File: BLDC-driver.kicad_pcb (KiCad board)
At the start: 2 copper layers, 52.2 x 52.2 mm, 107 parts, among them J1 Conn_01x06, J2 Conn_01x06, J3 Conn_01x02, J4 Encoder, Q1 FDMS8018, Q2 FDMS8018, Q3 FDMS8018, Q4 FDMS8018, Q5 FDMS8018, Q6 FDMS8018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

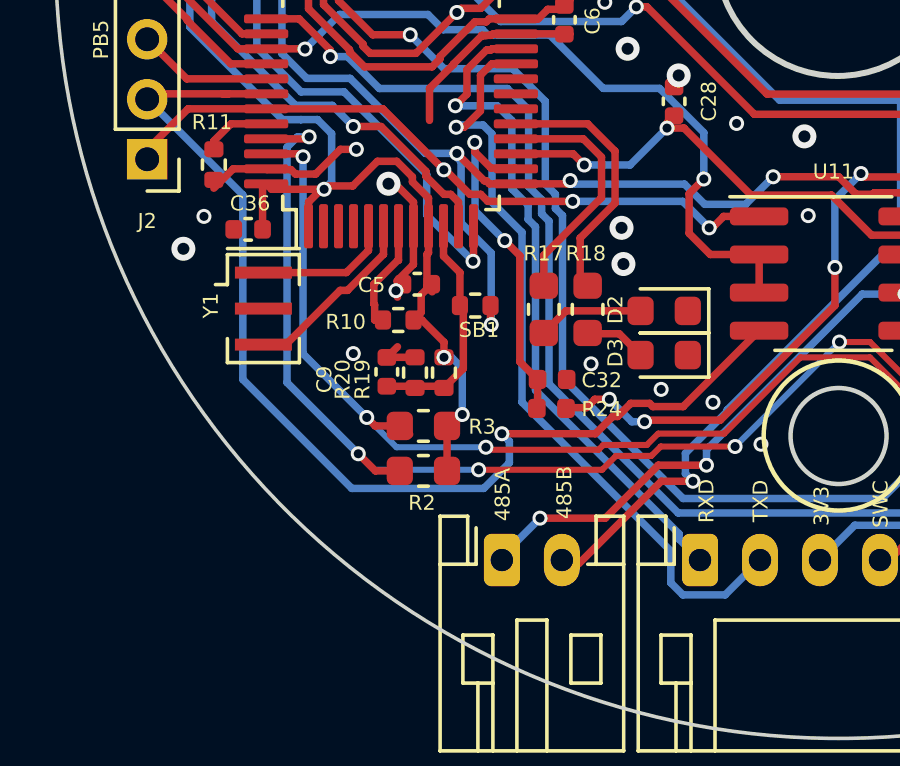
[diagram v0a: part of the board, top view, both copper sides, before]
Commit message: Update BOM, change crystal to 16Mhz
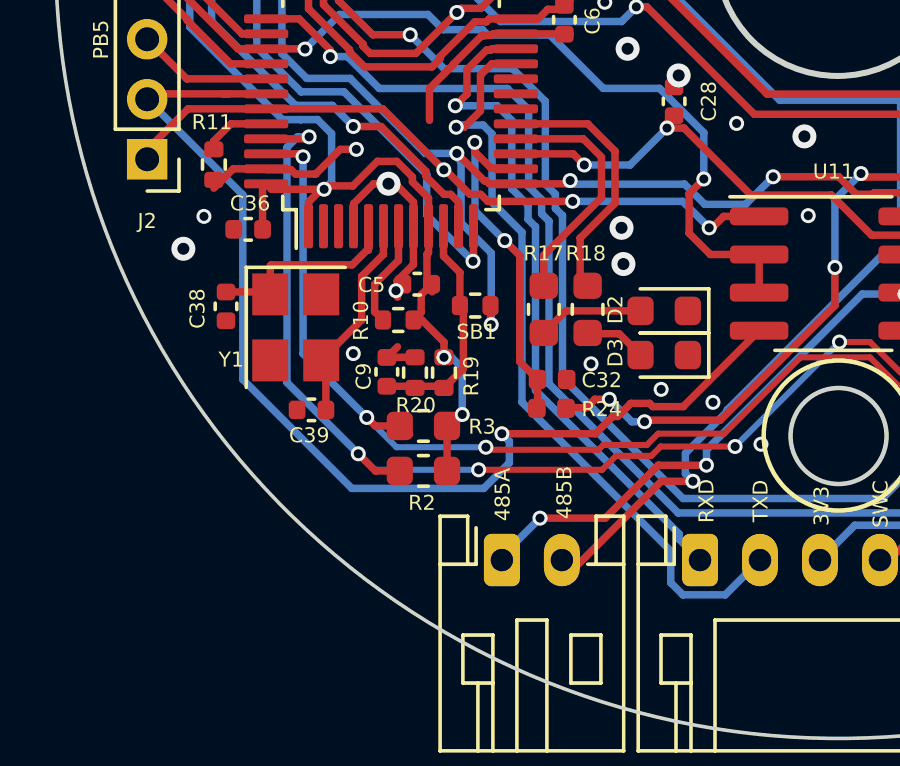
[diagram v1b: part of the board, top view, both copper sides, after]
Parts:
- added C38: 22p, Capacitor_SMD:C_0402_1005Metric, F.Cu at (176.3, 134.8)
- added C39: 22p, Capacitor_SMD:C_0402_1005Metric, F.Cu at (179.2, 138.3)
- Y1: value 8MHz -> 16MHz; footprint Crystal:Resonator_SMD_muRata_CSTxExxV-3Pin_3.0x1.1mm -> Crystal:Crystal_SMD_3225-4Pin_3.2x2.5mm
- moved Y1 1.25 mm to (178.6, 135.5)
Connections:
- U2 pad 18: Net-(U2-Pad18) -> (no net)
- U2 pad 19: Net-(U2-Pad19) -> (no net)
- U2 pad 2: Net-(U2-Pad2) -> (no net)
- U2 pad 20: Net-(U2-Pad20) -> (no net)
- U2 pad 25: Net-(U2-Pad25) -> (no net)
- U2 pad 26: Net-(U2-Pad26) -> (no net)
- U2 pad 3: Net-(U2-Pad3) -> (no net)
- U2 pad 32: /CANRX -> (no net)
- U2 pad 33: /CANTX -> (no net)
- U2 pad 4: Net-(U2-Pad4) -> GND
- U7 pad 4: Net-(U7-Pad4) -> (no net)
- Y1 pad 2: GND -> (no net)
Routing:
- net Net-(C38-Pad2): track 4.62 -> 7.52 mm
- net GND: track 54.5 -> 56.7 mm
- net Net-(C39-Pad2): track 6.19 -> 7.05 mm

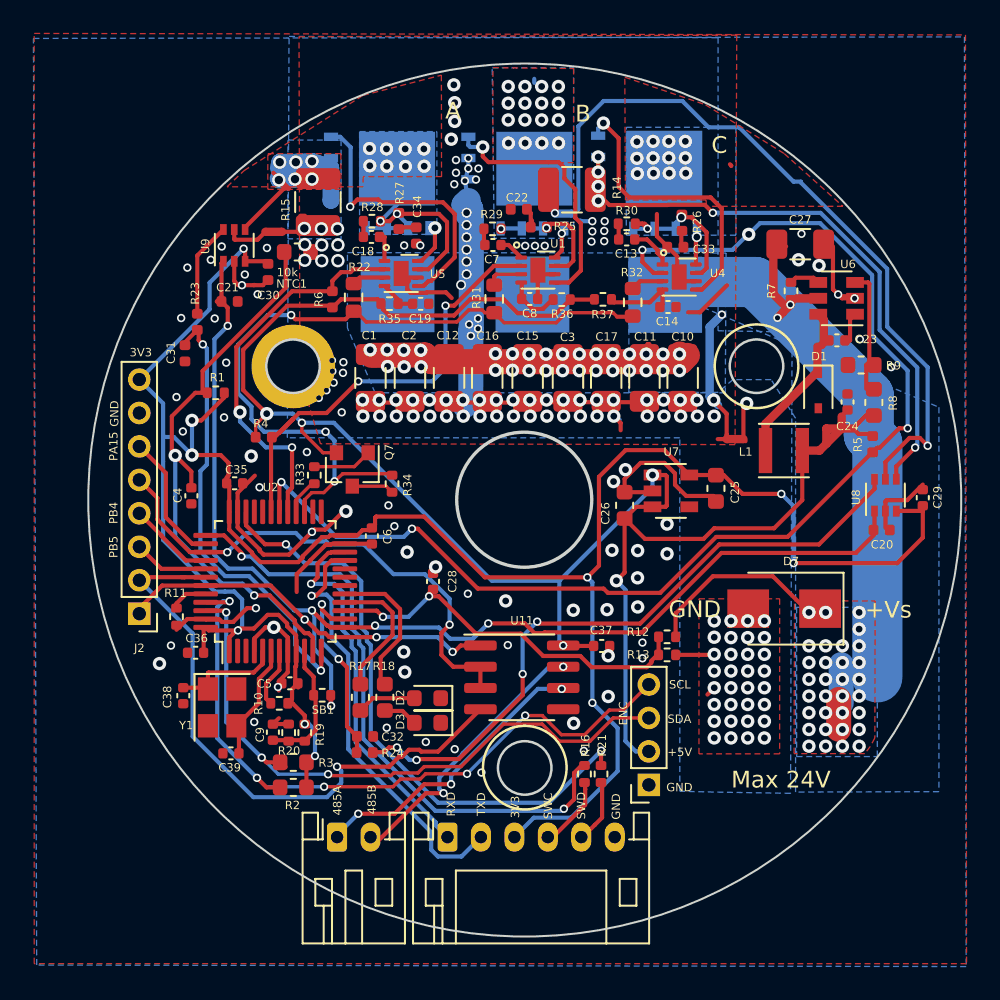
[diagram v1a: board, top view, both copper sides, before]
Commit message: Add encoder FFC connector, change NCP drivers to JLC sourceable
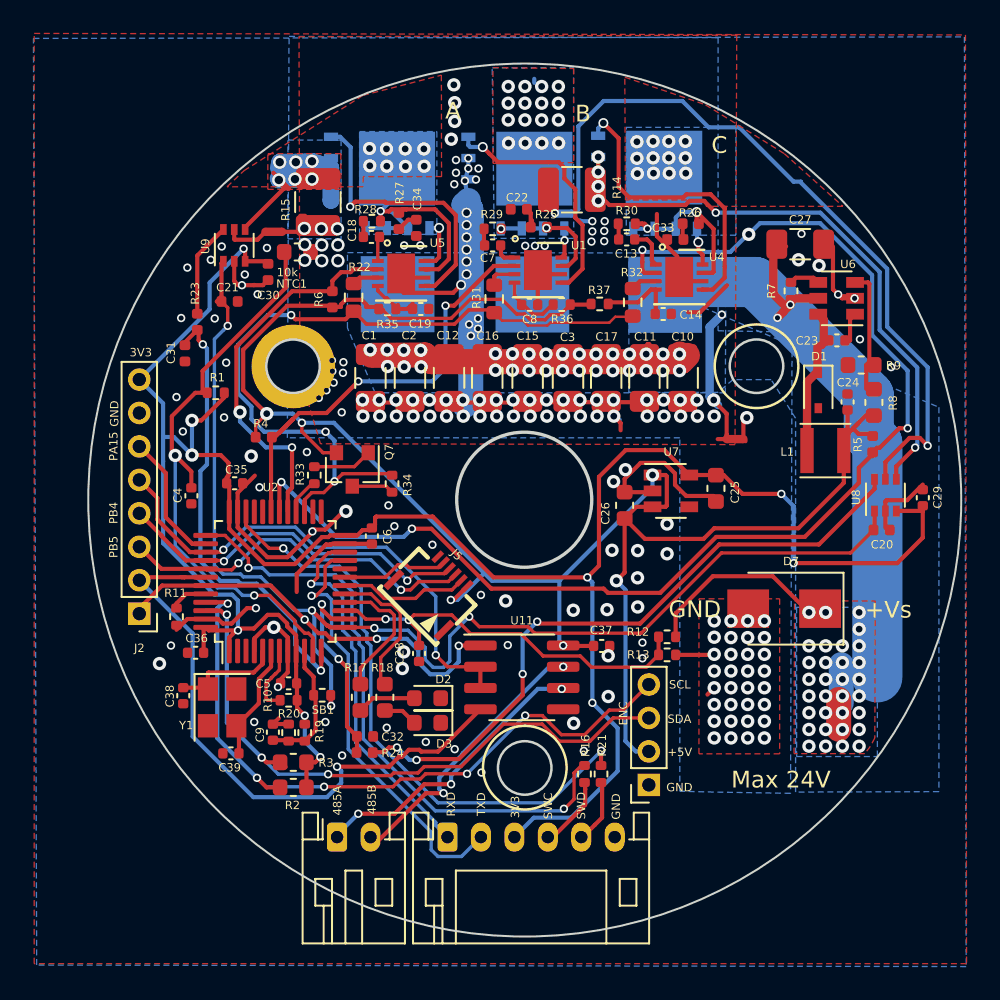
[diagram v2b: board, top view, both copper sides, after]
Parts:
- added J5: Conn_01x06, BLDC-Servo:FPC-SMD_F0502-B-06-10G-R, F.Cu at (191.4, 128.4)
- J1: value Conn_01x06 -> PROG/DBG
- J2: value Conn_01x06 -> DBG
- J3: value Conn_01x02 -> RS485
- U1, U4, U5: value NCP81151B -> NCP81155; footprint Package_DFN_QFN:DFN-8-1EP_2x2mm_P0.5mm_EP0.9x1.5mm -> Package_DFN_QFN:DFN-8-1EP_3x3mm_P0.5mm_EP1.66x2.38mm
- moved C28 4.39 mm to (190.4, 132.3), turned to 90 degrees
- moved L1 2.48 mm to (214.7, 120.2)
- moved R10 0.59 mm to (182.6, 135.1)
- moved R26 0.53 mm to (206.7, 106.6), turned to 0 degrees
- moved C14 0.50 mm to (205.0, 112.0)
- moved C34 0.45 mm to (190.2, 106.8)
- moved C33 0.45 mm to (205.7, 107.5)
- moved C8 0.35 mm to (197.0, 111.5)
- moved R35 0.35 mm to (188.5, 111.7)
- moved R37 0.34 mm to (201.2, 111.4)
- moved C19 0.31 mm to (190.5, 111.7)
- moved R36 0.30 mm to (198.9, 111.4)
- moved C5 0.08 mm to (182.6, 134.1)
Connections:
- net /PB4 renamed /MISO
- net /PB5 renamed /MOSI
- U2 pad 18: (no net) -> /~CS
- U2 pad 19: (no net) -> /SCK
- U2 pad 2: (no net) -> Net-(U2-Pad2)
- U2 pad 20: (no net) -> Net-(U2-Pad20)
- U2 pad 25: (no net) -> Net-(U2-Pad25)
- U2 pad 26: (no net) -> Net-(U2-Pad26)
- U2 pad 3: (no net) -> Net-(U2-Pad3)
- U2 pad 32: (no net) -> /CANRX
- U2 pad 33: (no net) -> /CANTX
- U7 pad 4: (no net) -> Net-(U7-Pad4)
- Y1 pad 2: (no net) -> Net-(Y1-Pad2)
- Y1 pad 4: (no net) -> Net-(Y1-Pad4)
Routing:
- net /MOSI: track 4.51 -> 21.8 mm, vias 0 -> 2
- net /MISO: track 5.15 -> 21.9 mm, vias 0 -> 2
- net /~CS: track 0.00 -> 7.73 mm
- net /SCK: track 0.00 -> 6.41 mm
- net +5V: track 115.0 -> 118.1 mm, vias 5 -> 6
- net /VREF_OUT: track 71.4 -> 74.5 mm
- net /U1_RX: track 22.6 -> 24.7 mm
- net /PH_B: track 12.4 -> 14.3 mm
- net /PH_C: track 15.9 -> 17.2 mm, vias 10 -> 9
- net Net-(C23-Pad1): track 10.9 -> 9.86 mm
- net Net-(C19-Pad1): track 2.23 -> 3.14 mm
- net GND: track 56.7 -> 55.8 mm, vias 61 -> 62
- net GNDPWR: track 67.9 -> 68.7 mm
- net /LG_A: track 15.6 -> 14.9 mm
- net /PH_A: track 7.95 -> 7.32 mm
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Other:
- copper layers 2 -> 4
- net class Default: clearance 0.16 -> 0.14
- rule trace_clearance: 0.16 -> 0.14
- rule trace_min: 0.2 -> 0.15

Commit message: Update JLC BOM
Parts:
- D1: value 30V -> 1N5819WS
- D7: value SMAJ24A -> SMAJ20A
- J5: value Conn_01x06 -> Encoder
- U11: value SN75176AD -> SP485EEN-L/TR
- U7: value MIC5504-3.3YM5 -> XC6206P332MR

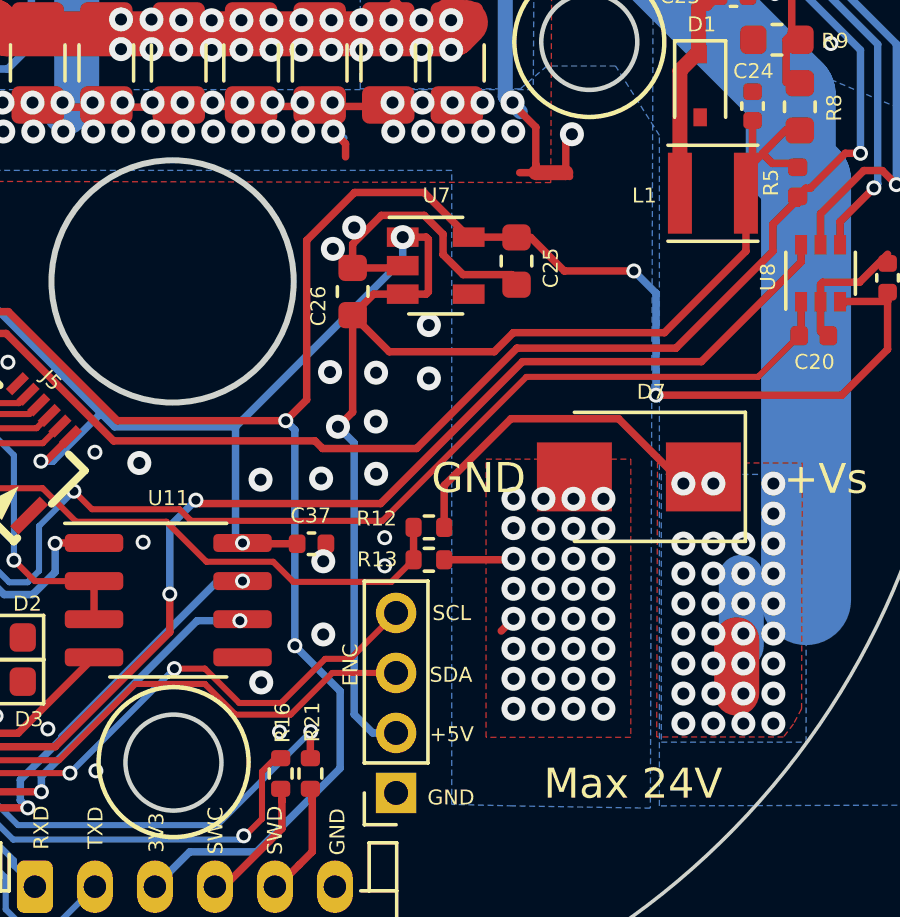
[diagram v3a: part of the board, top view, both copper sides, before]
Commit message: Update 3V3 LDO
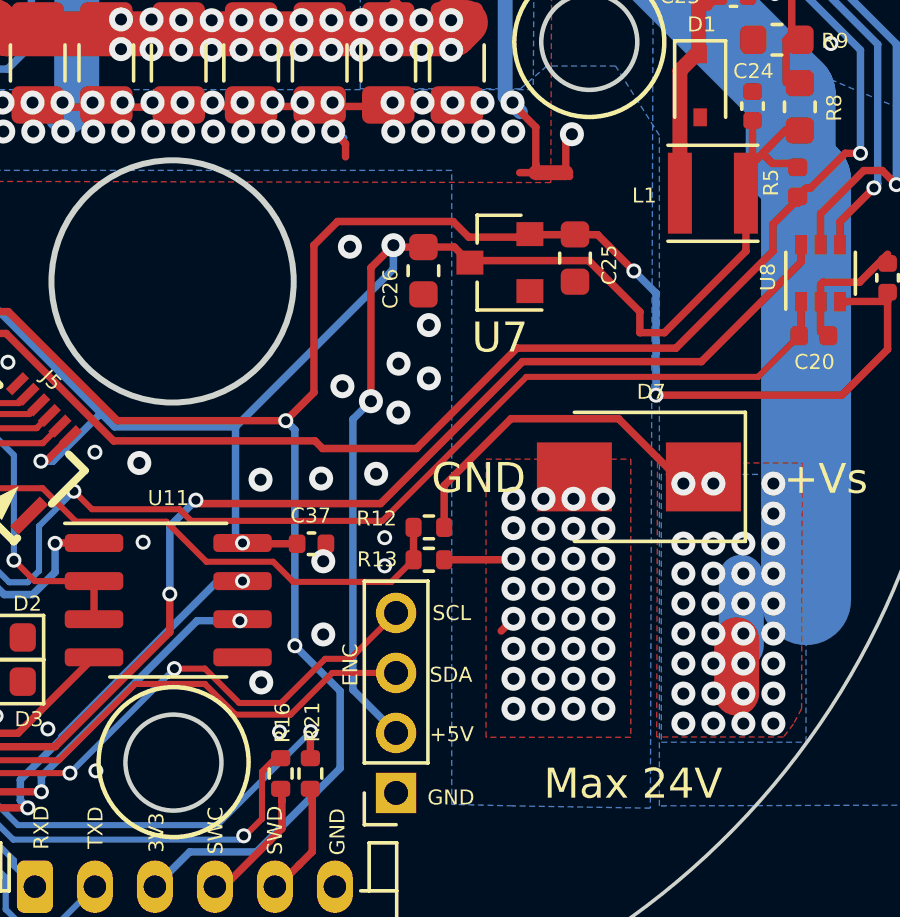
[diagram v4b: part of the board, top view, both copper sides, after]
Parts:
- U7: footprint Package_TO_SOT_SMD:SOT-23-5 -> Package_TO_SOT_SMD:SOT-23
- moved C26 2.46 mm to (205.1, 122.8), turned to 90 degrees
- moved U7 2.14 mm to (207.6, 122.5), turned to 180 degrees
- moved C25 1.95 mm to (210.1, 122.3)
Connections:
- U7 pad 1: +5V -> GND
- U7 pad 2: GND -> +3V3
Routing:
- net GND: track 55.8 -> 45.9 mm, vias 62 -> 61
- net +5V: track 118.1 -> 113.8 mm
- net +3V3: track 145.9 -> 145.0 mm

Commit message: Rev 4 update
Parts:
- added C40: 100uF, Capacitor_SMD:CP_Elec_8x6.5, F.Cu at (213.3, 128.6)
- added J6: PWR, Connector_JST:JST_VH_B2PS-VH_1x02_P3.96mm_Horizontal, F.Cu at (210.3, 139.4)
- C1, C10, C11, C12, C15, C16, C17, C2, C27, C3: value 10uF -> 22uF
- J5: value Encoder -> Encoder/SPI; footprint BLDC-Servo:FPC-SMD_F0502-B-06-10G-R -> JLC:FPC-SMD_F0502-B-06-10G-R
- moved D7 5.70 mm to (212.0, 135.3)
- moved C28 5.00 mm to (195.0, 130.4), turned to 180 degrees
- moved R1 1.73 mm to (176.7, 117.4)
- moved J1 1.02 mm to (192.2, 144.3)
- moved J3 1.02 mm to (185.6, 144.3)
- moved C20 0.89 mm to (218.9, 124.6)
- moved U8 0.71 mm to (218.8, 122.4)
- moved J5 0.50 mm to (191.1, 128.8)
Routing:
- net GND: track 45.9 -> 56.5 mm, vias 61 -> 69
- net GNDPWR: track 68.7 -> 73.1 mm, vias 127 -> 118
- net +24V: track 84.3 -> 88.5 mm
- net +3V3: track 145.0 -> 142.5 mm
- net /TXD: track 26.0 -> 27.9 mm
- net /485B: track 16.2 -> 18.0 mm
- net /485A: track 17.6 -> 19.3 mm
- net /RXD: track 22.5 -> 24.2 mm
- net /VREF_OUT: track 74.5 -> 76.2 mm
- net Net-(J1-Pad5): track 3.99 -> 5.53 mm
- net Net-(J1-Pad4): track 4.52 -> 5.93 mm
- net /PWM_C: track 23.0 -> 24.0 mm
- net /PHB_GND: track 44.7 -> 43.8 mm
- net /CURR_B: track 39.9 -> 40.7 mm
- net /VBUS: track 23.6 -> 24.3 mm
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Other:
- board text added: "FOC Drive Walmis@2022.02 REV4 www.ensys.lt"
- board text removed: "FOC Drive Walmis@2021.07 REV3 www.ensys.lt"

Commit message: Latest revision
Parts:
- added J7: Conn_01x04, Connector_PinHeader_2.00mm:PinHeader_1x04_P2.00mm_Vertical, F.Cu at (201.9, 120.1)
- J5: value Encoder/SPI -> Conn_01x04; footprint JLC:FPC-SMD_F0502-B-06-10G-R -> Connector_PinHeader_2.00mm:PinHeader_1x04_P2.00mm_Vertical
- Q1, Q2, Q3, Q4, Q5, Q6: footprint Package_TO_SOT_SMD:TDSON-8-1 -> JLC:FDMS8018
- U2: value STM32L412CB -> GD32F330C8T6
- moved J5 8.64 mm to (191.5, 120.1), turned to 0 degrees
- moved C23 0.89 mm to (216.3, 113.6)
- moved C24 0.89 mm to (216.9, 117.3)
- moved L1 0.89 mm to (215.6, 120.2)
- moved R5 0.89 mm to (218.4, 119.8)
- moved D1 0.89 mm to (215.2, 116.6)
- moved R8 0.89 mm to (218.5, 117.3)
- moved R9 0.89 mm to (217.7, 115.1)
- moved Q5 0.64 mm to (189.4, 110.4), turned to 0 degrees
- moved Q1 0.58 mm to (197.2, 110.4), turned to 0 degrees
- moved Q3 0.50 mm to (205.1, 110.3), turned to 0 degrees
- moved J6 0.44 mm to (210.3, 139.9)
- moved C18 0.44 mm to (187.6, 107.8)
- moved R28 0.44 mm to (187.6, 106.9)
- moved NT3 0.08 mm to (199.0, 105.9)
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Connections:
- J5 pad 1: +5V -> /~CS
- J5 pad 2: /~CS -> /MOSI
- J5 pad 3: /MOSI -> /MISO
- J5 pad 4: /MISO -> /SCK
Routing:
- net GND: track 56.5 -> 91.2 mm, vias 69 -> 67
- net GNDPWR: track 73.1 -> 90.9 mm, vias 118 -> 114
- net /~CS: track 7.73 -> 16.6 mm, vias 0 -> 1
- net /MOSI: track 22.0 -> 27.8 mm
- net /PH_A: track 7.99 -> 12.6 mm
- net /MISO: track 21.9 -> 25.2 mm
- net /PWM_B: track 75.2 -> 78.2 mm
- net +5V: track 113.7 -> 115.9 mm, vias 6 -> 5
- net +3V3: track 142.5 -> 144.6 mm, vias 10 -> 12
- net /PH_C: track 17.2 -> 15.4 mm, vias 9 -> 15
- net /HG_A: track 1.83 -> 0.88 mm
- net /PH_B: track 14.3 -> 15.2 mm, vias 14 -> 18
- net /U1_DE: track 30.1 -> 29.5 mm
- net /PHB_GND: track 43.8 -> 43.2 mm
- net /LG_C: track 17.2 -> 17.7 mm
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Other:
- copper layers 4 -> 2
- board text added: "CS"
- board text added: "MISO"
- board text added: "MOSI"
- board text added: "SCK"

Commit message: Rev 4
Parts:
- added H2: MountingHole_Pad, MountingHole:MountingHole_3.2mm_M3_DIN965_Pad_TopOnly, F.Cu at (210.6, 115.1)
- added H3: MountingHole_Pad, MountingHole:MountingHole_3.2mm_M3_DIN965_Pad_TopOnly, F.Cu at (196.7, 139.1)
- H1: footprint MountingHole:MountingHole_3.2mm_M3_DIN965_Pad -> MountingHole:MountingHole_3.2mm_M3_DIN965_Pad_TopOnly
- moved R16 1.34 mm to (200.9, 140.7)
- moved R21 1.34 mm to (201.9, 140.7)
- moved C4 0.90 mm to (177.1, 123.7), turned to 180 degrees
- moved J5 0.27 mm to (191.7, 120.1)
- moved J7 0.21 mm to (201.7, 120.1)
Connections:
- net /MISO renamed /SPI0_MISO
- net /MOSI renamed /SPI0_MOSI
- J2 pad 5: /U1_DE -> /SPI0_SCK
- J2 pad 6: /PA15 -> /SPI0_NSS
- J5 pad 1: /~CS -> /SPI0_NSS
- J5 pad 4: /SCK -> /SPI0_SCK
- U2 pad 18: /~CS -> Net-(U2-Pad18)
- U2 pad 19: /SCK -> Net-(U2-Pad19)
- U2 pad 20: Net-(U2-Pad20) -> /U1_DE
- U2 pad 3: Net-(U2-Pad3) -> GND
- U2 pad 38: /PA15 -> /SPI0_NSS
- U2 pad 39: /U1_DE -> /SPI0_SCK
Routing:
- net /SPI0_NSS: track 0.00 -> 25.2 mm, vias 0 -> 2
- net /SPI0_SCK: track 0.00 -> 23.0 mm, vias 0 -> 2
- net GNDPWR: track 90.9 -> 68.6 mm, vias 114 -> 115
- net /~CS: track 16.6 -> 0.00 mm, vias 1 -> 0
- net /U1_DE: track 29.5 -> 13.8 mm
- net GND: track 91.2 -> 79.2 mm, vias 67 -> 65
- net /PA15: track 7.93 -> 0.00 mm
- net /SCK: track 6.40 -> 0.00 mm
- net +24V: track 88.0 -> 93.6 mm, vias 65 -> 63
- net /PHB_SH: track 36.3 -> 39.4 mm
- net /FET_TEMP: track 34.4 -> 32.6 mm
- net Net-(J1-Pad5): track 5.53 -> 3.80 mm
- net Net-(J1-Pad4): track 5.93 -> 4.34 mm
- net +3V3: track 144.6 -> 143.1 mm
- net /PWM_B: track 78.2 -> 79.6 mm
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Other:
- outline, holes or cut-outs redrawn
- board text added: "NSS"
- board text removed: "PA15"
- board text removed: "PB4"
- board text removed: "PB5"
